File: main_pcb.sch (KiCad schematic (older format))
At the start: 56 parts, among them J1 STLink_conn, J10 Conn_01x03_Male, J11 Conn_02x02_Odd_Even, J12 Conn_01x09_Male, J13 Conn_Coaxial, J14 Conn_01x03_Male, J15 USB_conn, J2 Conn_01x04_Male, J3 Conn_02x03_Top_Bottom, J4 Conn_02x03_Top_Bottom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

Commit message: center
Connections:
- net at U1.25 (PB12): now also J12.8 (Pin_8); no longer J12.5 (Pin_5)
- net at U1.26 (PB13): now also J12.7 (Pin_7); no longer J12.6 (Pin_6)
- net at U1.27 (PB14): now also J12.6 (Pin_6); no longer J12.7 (Pin_7)
- net at U1.28 (PB15): now also J12.5 (Pin_5); no longer J12.8 (Pin_8)
- net at U1.45 (PB8): now also J12.2 (Pin_2); no longer J12.1 (Pin_1)
- net at U1.46 (PB9): now also J12.1 (Pin_1); no longer J12.2 (Pin_2)
- net at J2.2 (Pin_2): now also R3.2; no longer R2.2
- net at J2.3 (Pin_3): now also R2.2; no longer R3.2
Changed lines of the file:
@@
 $EndComp
-Wire Wire Line
-	1600 6500 2450 6500
-Wire Wire Line
-	1600 6600 2400 6600
 Wire Wire Line
 	2400 6600 2400 6650
@@
 spi1_mosi
 Wire Wire Line
-	5600 3850 6900 3850
-Wire Wire Line
-	6900 3950 5600 3950
-Wire Wire Line
 	5600 4050 6900 4050
 Wire Wire Line
 	5600 4150 6900 4150
-Wire Wire Line
-	5600 4250 6900 4250
-Wire Wire Line
-	6900 4350 5600 4350
-Wire Wire Line
-	5600 4450 6900 4450
-Wire Wire Line
-	6900 4550 5600 4550
 NoConn ~ 2350 2950
 NoConn ~ 2350 3050
@@
 Wire Wire Line
 	3650 850  4200 850
+Wire Wire Line
+	6900 4250 6000 4250
+Wire Wire Line
+	6000 4250 6000 4550
+Wire Wire Line
+	6000 4550 5600 4550
+Wire Wire Line
+	5600 4250 5850 4250
+Wire Wire Line
+	5850 4250 5850 4600
+Wire Wire Line
+	5850 4600 6400 4600
+Wire Wire Line
+	6400 4600 6400 4550
+Wire Wire Line
+	6400 4550 6900 4550
+Wire Wire Line
+	5600 4450 6400 4450
+Wire Wire Line
+	6400 4450 6400 4350
+Wire Wire Line
+	6400 4350 6900 4350
+Wire Wire Line
+	6450 4450 6450 4400
+Wire Wire Line
+	6450 4400 5750 4400
+Wire Wire Line
+	5750 4400 5750 4350
+Wire Wire Line
+	5750 4350 5600 4350
+Wire Wire Line
+	6450 4450 6900 4450
+Wire Wire Line
+	5600 3850 6550 3850
+Wire Wire Line
+	6550 3850 6550 3950
+Wire Wire Line
+	6550 3950 6900 3950
+Wire Wire Line
+	6900 3850 6650 3850
+Wire Wire Line
+	6650 3850 6650 3900
+Wire Wire Line
+	6650 3900 6100 3900
+Wire Wire Line
+	6100 3900 6100 3950
+Wire Wire Line
+	6100 3950 5600 3950
+Wire Wire Line
+	1600 6500 2250 6500
+Wire Wire Line
+	2250 6500 2250 6600
+Wire Wire Line
+	2250 6600 2400 6600
+Wire Wire Line
+	2450 6500 2350 6500
+Wire Wire Line
+	2350 6500 2350 6550
+Wire Wire Line
+	2350 6550 2000 6550
+Wire Wire Line
+	2000 6550 2000 6600
+Wire Wire Line
+	2000 6600 1600 6600
 $EndSCHEMATC

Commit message: work PC
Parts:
- removed J3: Conn_02x03_Top_Bottom, Pin_Headers:Pin_Header_Straight_2x03_Pitch2.54mm, symbol Connector_Generic:Conn_02x03_Top_Bottom
- added J3: Conn_02x03_Odd_Even, Connector_PinHeader_2.54mm:PinHeader_2x03_P2.54mm_Vertical, symbol Connector_Generic:Conn_02x03_Odd_Even
- U1: footprint Housings_QFP:LQFP-48_7x7mm_Pitch0.5mm -> Package_QFP:LQFP-48_7x7mm_P0.5mm
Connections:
- net 3v3_STLink: now also J3.2 (Pin_2)
- net AMS1117_3v3: now also J3.4 (Pin_4)
- net UART_FW: now also J3.6 (Pin_6)
- net VCC: now also J3.1 (Pin_1), J3.3 (Pin_3), J3.5 (Pin_5)
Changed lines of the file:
@@
 F 0 "U1" H 7600 3250 50  0000 C CNN
 F 1 "STM32F103C8Tx" H 7600 3150 50  0000 C CNN
-F 2 "Housings_QFP:LQFP-48_7x7mm_Pitch0.5mm" H 7000 1850 50  0001 R CNN
+F 2 "Package_QFP:LQFP-48_7x7mm_P0.5mm" H 7000 1850 50  0001 R CNN
 F 3 "http://www.st.com/st-web-ui/static/active/en/resource/technical/document/datasheet/CD00161566.pdf" H 7600 3250 50  0001 C CNN
 	1    7600 3250
@@
 	1000 3850 800  3850
 $Comp
-L Connector_Generic:Conn_02x03_Top_Bottom J3
-U 1 1 5E71B824
-P 1450 6000
-F 0 "J3" H 1500 6317 50  0000 C CNN
-F 1 "Conn_02x03_Top_Bottom" H 1500 6226 50  0000 C CNN
-F 2 "Pin_Headers:Pin_Header_Straight_2x03_Pitch2.54mm" H 1450 6000 50  0001 C CNN
-F 3 "~" H 1450 6000 50  0001 C CNN
-	1    1450 6000
-	1    0    0    -1
-$EndComp
-$Comp
 L power:VCC #PWR02
 U 1 1 5E71C780
@@
 $EndComp
 Wire Wire Line
-	1250 6100 900  6100
-Wire Wire Line
 	900  6100 900  6000
-Wire Wire Line
-	1250 5900 1100 5900
 Connection ~ 900  5900
 Wire Wire Line
 	900  5900 900  5800
-Wire Wire Line
-	1250 6000 900  6000
 Connection ~ 900  6000
 Wire Wire Line
@@
 Text Label 1750 4900 0    50   ~ 0
 3v3_STLink
-Text Label 1750 5900 0    50   ~ 0
+Text Label 2150 5900 0    50   ~ 0
 3v3_STLink
 Text Label 10250 1950 0    50   ~ 0
 AMS1117_3v3
-Text Label 1750 6000 0    50   ~ 0
+Text Label 2150 6000 0    50   ~ 0
 AMS1117_3v3
 $Comp
@@
 Wire Wire Line
 	1600 6700 2150 6700
-Text Label 1750 6100 0    50   ~ 0
+Text Label 2150 6100 0    50   ~ 0
 UART_FW
 $Comp
@@
 Wire Wire Line
 	2000 6600 1600 6600
+$Comp
+L Connector_Generic:Conn_02x03_Odd_Even J3
+U 1 1 5E6867AD
+P 1500 6000
+F 0 "J3" H 1550 6317 50  0000 C CNN
+F 1 "Conn_02x03_Odd_Even" H 1550 6226 50  0000 C CNN
+F 2 "Connector_PinHeader_2.54mm:PinHeader_2x03_P2.54mm_Vertical" H 1500 6000 50  0001 C CNN
+F 3 "~" H 1500 6000 50  0001 C CNN
+	1    1500 6000
+	1    0    0    -1
+$EndComp
+Wire Wire Line
+	1100 5900 1300 5900
+Wire Wire Line
+	900  6000 1300 6000
+Wire Wire Line
+	900  6100 1300 6100
+Wire Wire Line
+	1800 5900 2150 5900
+Wire Wire Line
+	1800 6000 2150 6000
+Wire Wire Line
+	1800 6100 2150 6100
 $EndSCHEMATC

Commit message: work PC
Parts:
- removed J4: Conn_02x03_Top_Bottom, Pin_Headers:Pin_Header_Straight_2x03_Pitch2.54mm, symbol Connector_Generic:Conn_02x03_Top_Bottom
- added J4: Conn_02x03_Odd_Even, Connector_PinHeader_2.54mm:PinHeader_2x03_P2.54mm_Vertical, symbol Connector_Generic:Conn_02x03_Odd_Even
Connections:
- net BOOT0: now also J4.3 (Pin_3)
- net BOOT1: now also J4.4 (Pin_4)
- net GND: now also J4.5 (Pin_5), J4.6 (Pin_6)
- net VCC: now also J4.1 (Pin_1), J4.2 (Pin_2)
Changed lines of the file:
@@
 Connection ~ 8300 1450
-$Comp
-L Connector_Generic:Conn_02x03_Top_Bottom J4
-U 1 1 5E4B4AFA
-P 1450 7250
-F 0 "J4" H 1500 7567 50  0000 C CNN
-F 1 "Conn_02x03_Top_Bottom" H 1500 7476 50  0000 C CNN
-F 2 "Pin_Headers:Pin_Header_Straight_2x03_Pitch2.54mm" H 1450 7250 50  0001 C CNN
-F 3 "~" H 1450 7250 50  0001 C CNN
-	1    1450 7250
-	1    0    0    -1
-$EndComp
 $Comp
 L power:VCC #PWR03
@@
 Wire Wire Line
 	1800 6100 2150 6100
+$Comp
+L Connector_Generic:Conn_02x03_Odd_Even J4
+U 1 1 5E6F7C0A
+P 1450 7250
+F 0 "J4" H 1500 7567 50  0000 C CNN
+F 1 "Conn_02x03_Odd_Even" H 1500 7476 50  0000 C CNN
+F 2 "Connector_PinHeader_2.54mm:PinHeader_2x03_P2.54mm_Vertical" H 1450 7250 50  0001 C CNN
+F 3 "~" H 1450 7250 50  0001 C CNN
+	1    1450 7250
+	1    0    0    -1
+$EndComp
 $EndSCHEMATC

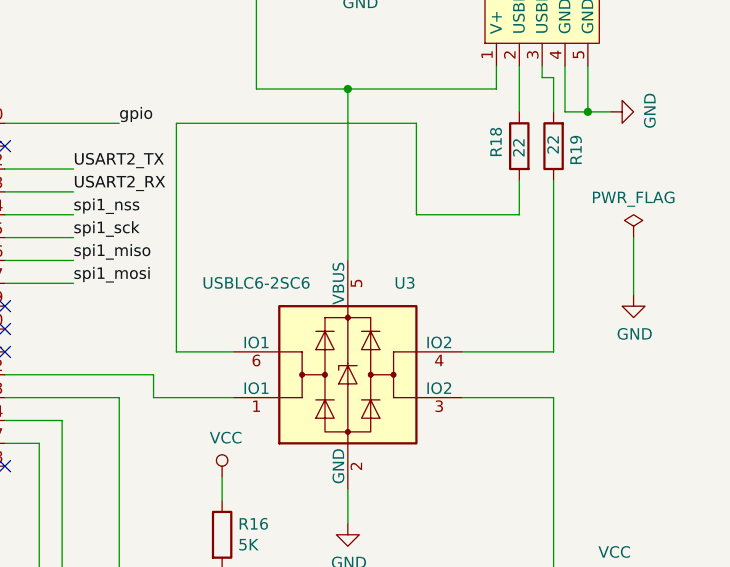
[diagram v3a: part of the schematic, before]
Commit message: stm32 is bootom, rhf78 is top
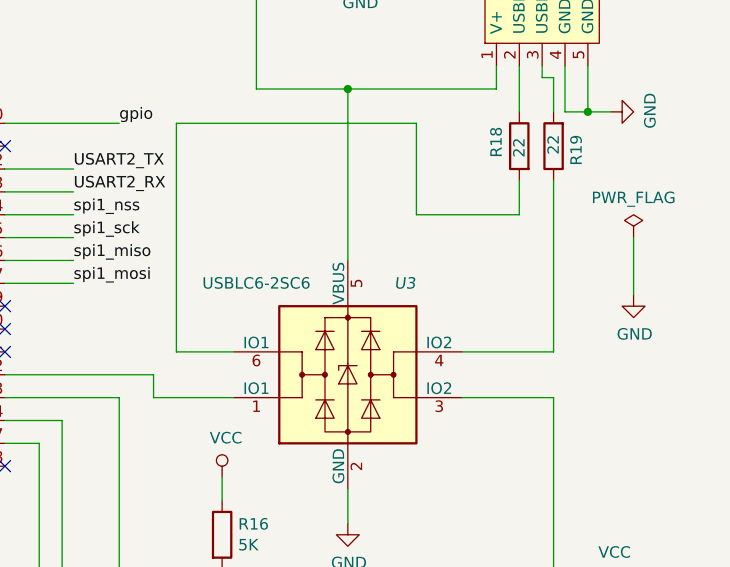
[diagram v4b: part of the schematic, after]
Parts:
- J3, J4: footprint Connector_PinHeader_2.54mm:PinHeader_2x03_P2.54mm_Vertical -> Pin_Headers:Pin_Header_Straight_2x03_Pitch2.54mm
- U1: footprint Package_QFP:LQFP-48_7x7mm_P0.5mm -> Housings_QFP:LQFP-48_7x7mm_Pitch0.5mm
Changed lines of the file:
@@
 F 0 "U1" H 7600 3250 50  0000 C CNN
 F 1 "STM32F103C8Tx" H 7600 3150 50  0000 C CNN
-F 2 "Package_QFP:LQFP-48_7x7mm_P0.5mm" H 7000 1850 50  0001 R CNN
+F 2 "Housings_QFP:LQFP-48_7x7mm_Pitch0.5mm" H 7000 1850 50  0001 R CNN
 F 3 "http://www.st.com/st-web-ui/static/active/en/resource/technical/document/datasheet/CD00161566.pdf" H 7600 3250 50  0001 C CNN
 	1    7600 3250
@@
 U 1 1 5E530E7D
 P 9700 4150
-F 0 "U3" H 9950 4550 50  0000 C CNN
+F 0 "U3" H 9950 4550 50  0000 C CIN
 F 1 "USBLC6-2SC6" H 9300 4550 50  0000 C CNN
 F 2 "TO_SOT_Packages_SMD:SOT-23-6_Handsoldering" H 8950 4550 50  0001 C CNN
@@
 F 0 "J3" H 1550 6317 50  0000 C CNN
 F 1 "Conn_02x03_Odd_Even" H 1550 6226 50  0000 C CNN
-F 2 "Connector_PinHeader_2.54mm:PinHeader_2x03_P2.54mm_Vertical" H 1500 6000 50  0001 C CNN
+F 2 "Pin_Headers:Pin_Header_Straight_2x03_Pitch2.54mm" H 1500 6000 50  0001 C CNN
 F 3 "~" H 1500 6000 50  0001 C CNN
 	1    1500 6000
@@
 F 0 "J4" H 1500 7567 50  0000 C CNN
 F 1 "Conn_02x03_Odd_Even" H 1500 7476 50  0000 C CNN
-F 2 "Connector_PinHeader_2.54mm:PinHeader_2x03_P2.54mm_Vertical" H 1450 7250 50  0001 C CNN
+F 2 "Pin_Headers:Pin_Header_Straight_2x03_Pitch2.54mm" H 1450 7250 50  0001 C CNN
 F 3 "~" H 1450 7250 50  0001 C CNN
 	1    1450 7250

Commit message: work PC
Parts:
- C1, C2, C3, C4, C5, C6, C7, C8, C9: footprint Capacitors_SMD:C_0805_HandSoldering -> LoraWAN_pcb:C_0805_HandSoldering
- D1, D3, D4, D5: footprint LEDs:LED_0805_HandSoldering -> LoraWAN_pcb:LED_0805_HandSoldering
- D2: footprint RHF78_footprint:RHF78_052 -> LoraWAN_pcb:RHF78_052
- J1: footprint Pin_Headers:Pin_Header_Straight_1x05_Pitch2.54mm -> LoraWAN_pcb:Pin_Header_Straight_1x05_Pitch2.54mm
- J10, J14, J6, J7: footprint Pin_Headers:Pin_Header_Straight_1x03_Pitch2.54mm -> LoraWAN_pcb:Pin_Header_Straight_1x03_Pitch2.54mm
- J11: footprint Pin_Headers:Pin_Header_Straight_2x02_Pitch2.54mm -> LoraWAN_pcb:Pin_Header_Straight_2x02_Pitch2.54mm
- J12: footprint Pin_Headers:Pin_Header_Straight_1x09_Pitch2.54mm -> LoraWAN_pcb:Pin_Header_Straight_1x09_Pitch2.54mm
- J13: footprint U_FL_smd:U_FL_smd -> LoraWAN_pcb:U_FL_smd
- J15: footprint Connectors:USB_Micro-B -> LoraWAN_pcb:USB_Micro-B
- J2: footprint Pin_Headers:Pin_Header_Straight_1x04_Pitch2.54mm -> LoraWAN_pcb:Pin_Header_Straight_1x04_Pitch2.54mm
- J3, J4: footprint Pin_Headers:Pin_Header_Straight_2x03_Pitch2.54mm -> LoraWAN_pcb:Pin_Header_Straight_2x03_Pitch2.54mm
- J5, J9: footprint Pin_Headers:Pin_Header_Straight_1x01_Pitch2.54mm -> LoraWAN_pcb:Pin_Header_Straight_1x01_Pitch2.54mm
- J8: footprint Pin_Headers:Pin_Header_Straight_1x06_Pitch2.54mm -> LoraWAN_pcb:Pin_Header_Straight_1x06_Pitch2.54mm
- R1, R10, R11, R12, R13, R14, R15, R16, R18, R19, R2, R3, R4, R5, R6, R7, R8, R9: footprint Resistors_SMD:R_0805_HandSoldering -> LoraWAN_pcb:R_0805_HandSoldering
- R17: footprint Potentiometers:Potentiometer_Trimmer_Bourns_3296W -> LoraWAN_pcb:Potentiometer_Trimmer_Bourns_3296W
- SW1, SW2: footprint Buttons_Switches_SMD:SW_SPST_EVQPE1 -> LoraWAN_pcb:SW_SPST_EVQPE1
- U1: footprint Housings_QFP:LQFP-48_7x7mm_Pitch0.5mm -> LoraWAN_pcb:LQFP-48_7x7mm_Pitch0.5mm
- U2: footprint Housings_SOIC:SOIC-8_3.9x4.9mm_Pitch1.27mm -> LoraWAN_pcb:SOIC-8_3.9x4.9mm_Pitch1.27mm
- U3: footprint TO_SOT_Packages_SMD:SOT-23-6_Handsoldering -> LoraWAN_pcb:SOT-23-6_Handsoldering
- U4: footprint TO_SOT_Packages_SMD:SOT-223-3_TabPin2 -> LoraWAN_pcb:SOT-223-3_TabPin2
- Y1: footprint Crystals:Crystal_HC18-U_Vertical -> LoraWAN_pcb:Crystal_HC18-U_Vertical
- Y2: footprint Crystals:Crystal_AT310_d3.0mm_l10.0mm_Vertical -> LoraWAN_pcb:Crystal_AT310_d3.0mm_l10.0mm_Vertical

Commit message: board trace is finished
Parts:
- removed J12: Conn_01x09_Male, LoraWAN_pcb:Pin_Header_Straight_1x09_Pitch2.54mm, symbol main_pcb-rescue:Conn_01x09_Male-Connector
- removed J4: Conn_02x03_Odd_Even, LoraWAN_pcb:Pin_Header_Straight_2x03_Pitch2.54mm, symbol Connector_Generic:Conn_02x03_Odd_Even
- removed R12: 100K, LoraWAN_pcb:R_0805_HandSoldering, symbol Device:R
- added J12: Conn_01x01_Male, LoraWAN_pcb:Pin_Header_Straight_1x01_Pitch2.54mm, symbol Connector:Conn_01x01_Male
- added J4: Conn_01x03_Male, LoraWAN_pcb:Pin_Header_Straight_1x03_Pitch2.54mm, symbol Connector:Conn_01x03_Male
- R11: value 100K -> 5K
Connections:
- net BOOT1 is gone; now on an unnamed net: R11.1
- net GND: now also R11.2, U1.44 (BOOT0)
- net at U1.20 (PB2): no longer R11.2
- net at U1.25 (PB12): now also J4.1 (Pin_1)
- net at U1.26 (PB13): now also J4.2 (Pin_2)
- net at U1.27 (PB14): now also J4.3 (Pin_3)
- net 3VB: no longer names the net of U1.1 (VBAT)
- net 3VB: now also J12.1 (Pin_1)
- no-connect marks 15 -> 20
